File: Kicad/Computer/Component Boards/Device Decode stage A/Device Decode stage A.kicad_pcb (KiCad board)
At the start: 2 copper layers, 26.7 x 59.7 mm, 26 parts, among them IC1 AP7365-33WG-7, IC12 SN74LVC1G10DBVR, IC13 74LVC04APW,118, IC16 74LVC02APW,118, IC2 74LVC138APW-Q100J, IC3 74LVC02APW,118, IC4 74LVC1G32GV,125, IC5 74LVC02APW,118, IC6 74LVC3G34DP,125, IC7 SN74F521NSR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

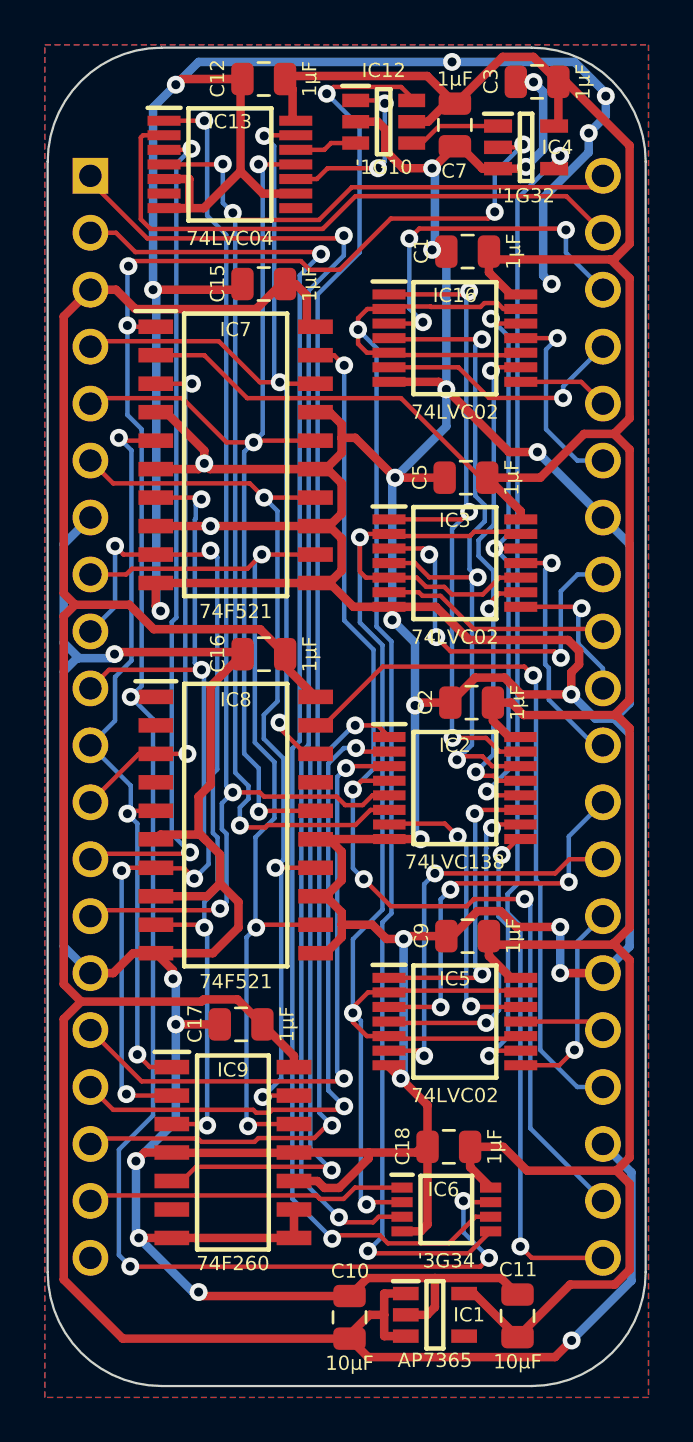
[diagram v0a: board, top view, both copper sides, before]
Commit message: Added Device Decode stage B.
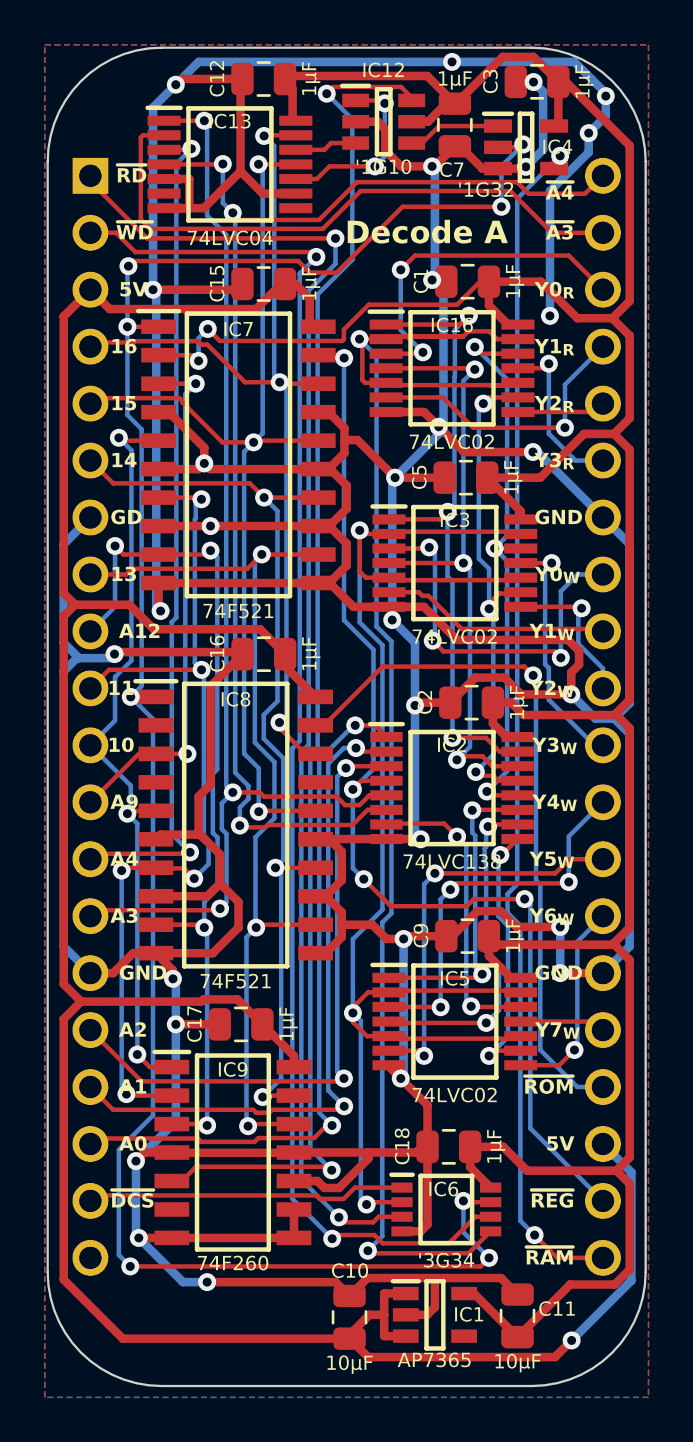
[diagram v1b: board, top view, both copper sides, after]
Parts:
- moved IC16 1.35 mm to (105.0, 67.0)
- moved C1 1.34 mm to (105.7, 63.1)
- moved IC2 0.13 mm to (105.0, 85.7)
- moved IC7 0.13 mm to (95.5, 70.9)
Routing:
- net /~{RD}: track 63.9 -> 67.9 mm
- net /Y1: track 31.3 -> 28.2 mm
- net /GND: track 384.5 -> 382.4 mm
- net /Y0: track 31.0 -> 29.1 mm
- net /Y2: track 24.3 -> 22.6 mm
- net /~{Y3+R}: track 9.03 -> 7.49 mm
- net /~{Y1+R}: track 11.4 -> 12.8 mm
- net /3.3V: track 144.9 -> 145.8 mm, vias 0 -> 2
- net /~{RD}_{IN}: track 60.7 -> 60.0 mm
- net /~{Device RAM}: track 54.4 -> 53.8 mm
- net /~{Y2+R}: track 4.07 -> 3.42 mm
- net /Y3: track 26.5 -> 25.9 mm
- net /~{Y0+R}: track 16.1 -> 15.7 mm, vias 3 -> 2
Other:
- board text added: "10"
- board text added: "11"
- board text added: "13"
- board text added: "14"
- board text added: "15"
- board text added: "16"
- board text added: "5V"
- board text added: "A0"
- board text added: "A1"
- board text added: "A12"
- board text added: "A2"
- board text added: "A3"
- board text added: "A4"
- board text added: "A9"
- board text added: "Decode A"
- board text added: "GD"
- board text added: "GND"
- board text added: "Y0_{R}"
- board text added: "Y0_{W}"
- board text added: "Y1_{R}"
- board text added: "Y1_{W}"
- board text added: "Y2_{R}"
- board text added: "Y2_{W}"
- board text added: "Y3_{R}"
- board text added: "Y3_{W}"
- board text added: "Y4_{W}"
- board text added: "Y5_{W}"
- board text added: "Y6_{W}"
- board text added: "Y7_{W}"
- board text added: "~{A3}"
- board text added: "~{A4}"
- board text added: "~{DCS}"
- board text added: "~{RAM}"
- board text added: "~{RD}"
- board text added: "~{REG}"
- board text added: "~{ROM}"
- board text added: "~{WD}"

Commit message: Bit of device decode fix-up.
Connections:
- net /Y0 renamed /~{Y0}
- net /Y1 renamed /~{Y1}
- net /Y2 renamed /~{Y2}
- net /Y3 renamed /~{Y3}
- net /Y4 renamed /~{Y4}
- net /Y5 renamed /~{Y5}
- net /Y6 renamed /~{Y6}
- net /Y7 renamed /~{Y7}
- net /~{Y0+R} renamed /Y0+R
- net /~{Y0+W} renamed /Y0+W
- net /~{Y1+R} renamed /Y1+R
- net /~{Y1+W} renamed /Y1+W
- net /~{Y2+R} renamed /Y2+R
- net /~{Y2+W} renamed /Y2+W
- net /~{Y3+R} renamed /Y3+R
- net /~{Y3+W} renamed /Y3+W
- net /~{Y4+W} renamed /Y4+W
- net /~{Y5+W} renamed /Y5+W
- net /~{Y6+W} renamed /Y6+W
- net /~{Y7+W} renamed /Y7+W

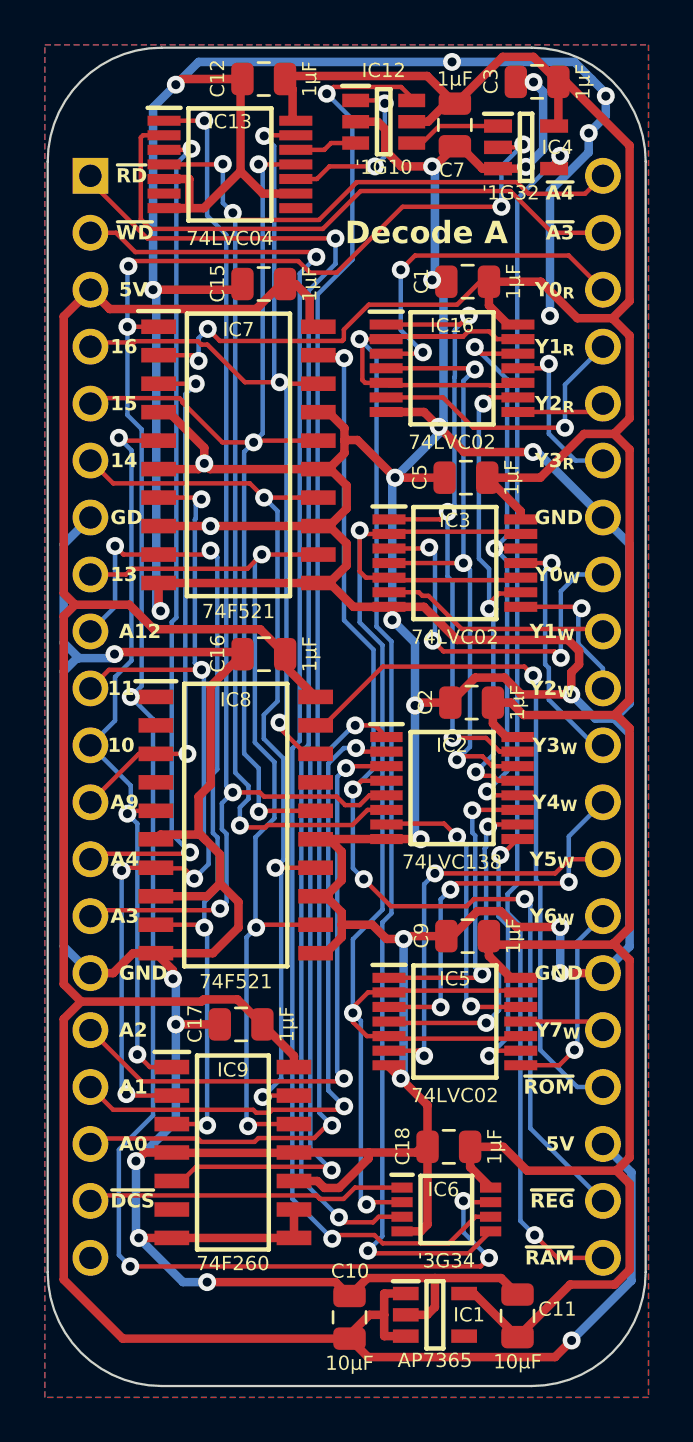
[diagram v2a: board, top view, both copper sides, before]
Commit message: Updated the Signal Buffer to be a Data and Signal Buffer.
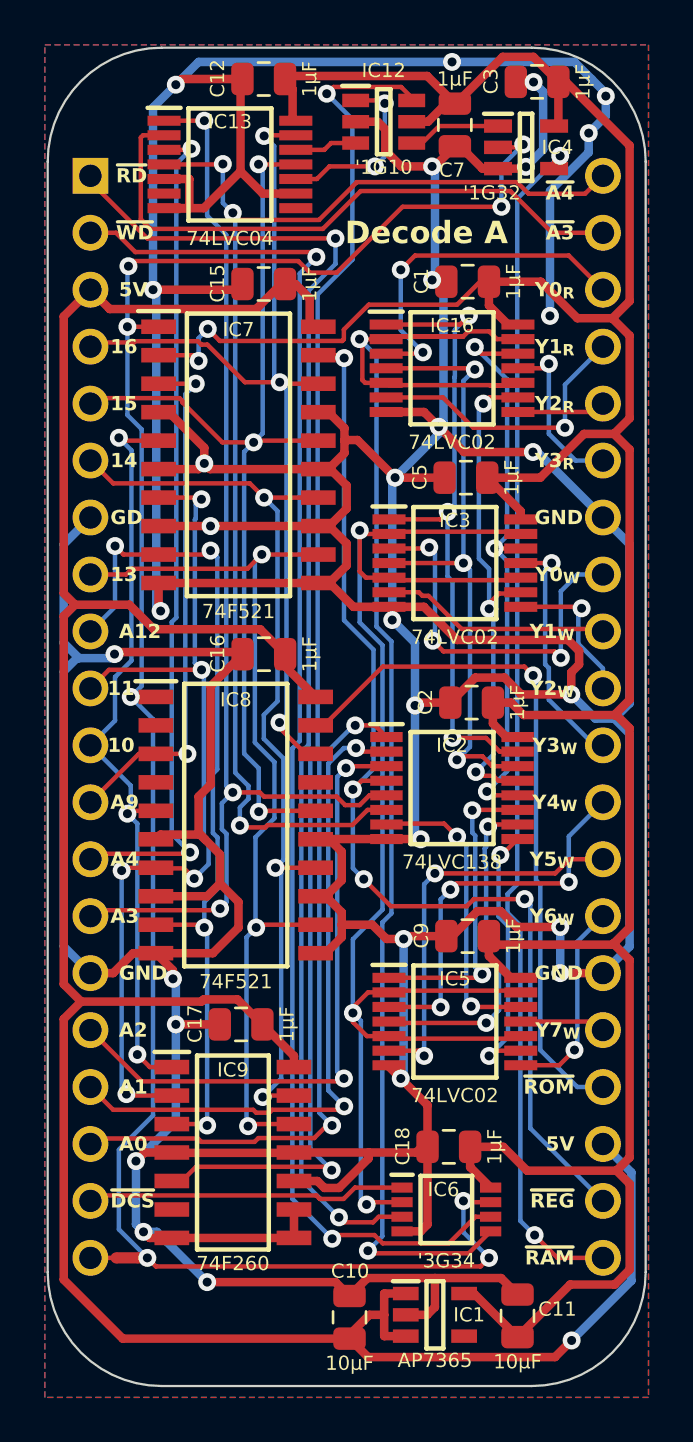
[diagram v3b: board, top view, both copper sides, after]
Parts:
- added NT1: NetTie_2, NetTie:NetTie-2_SMD_Pad0.5mm, F.Cu at (90.6, 106.7)
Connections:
- J1 pad 20: unconnected-(J1-Pin_20-Pad20) -> /~{Device Select} _{OUT}
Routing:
- net /~{Device Select} _{OUT}: track 0.00 -> 1.15 mm

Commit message: Include ROM read and write clock holds.
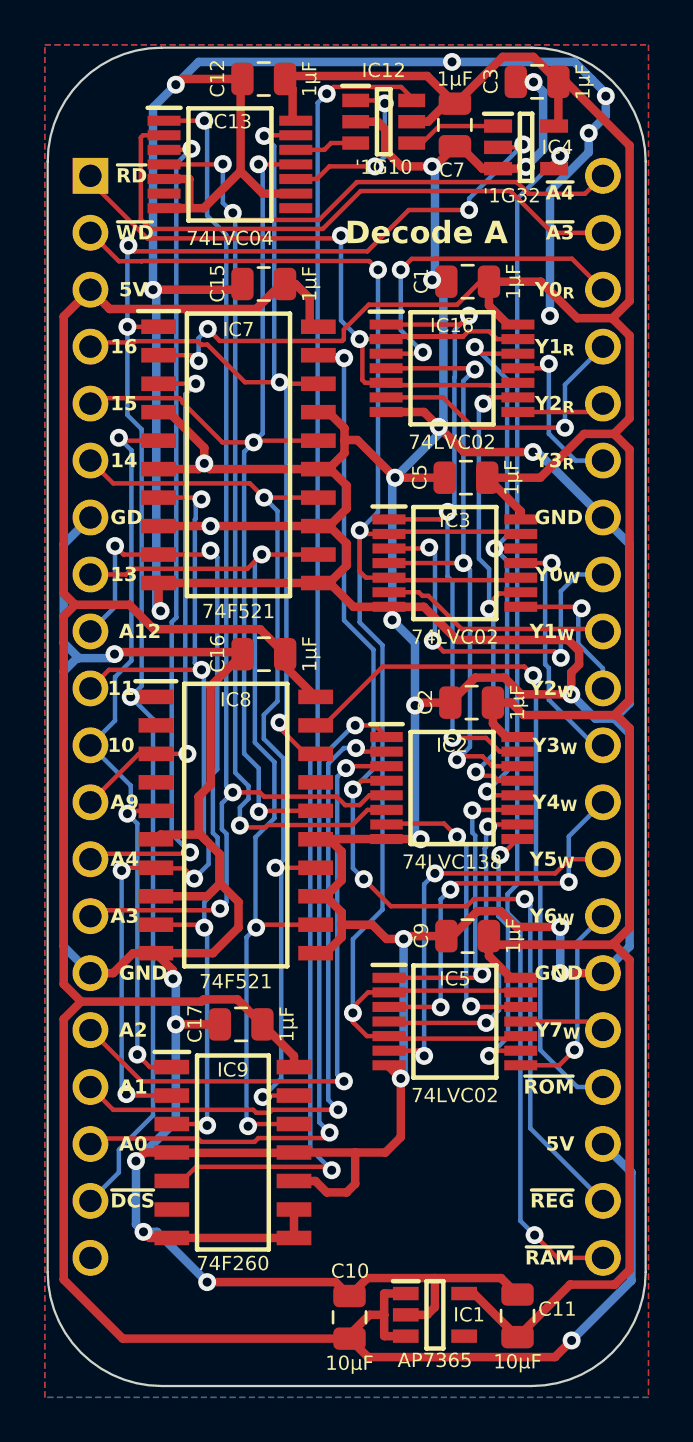
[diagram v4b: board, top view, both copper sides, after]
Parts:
- removed C18: 1μF, SamacSys_Parts:C_0805
- removed IC6: 74LVC3G34DP,125, SamacSys_Parts:SOP65P400X110-8N
- removed NT1: NetTie_2, NetTie:NetTie-2_SMD_Pad0.5mm
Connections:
- J1 pad 1: /~{RD}_{IN} -> /~{RD}
- J1 pad 19: /~{Device Select}_{ IN} -> /~{Device Select}
- J1 pad 2: /~{WD}_{IN} -> /~{WD}
- J1 pad 20: /~{Device Select} _{OUT} -> unconnected-(J1-Pin_20-Pad20)
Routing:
- net /~{WD}_{IN}: track 63.3 -> 0.00 mm, vias 2 -> 0
- net /~{RD}_{IN}: track 60.0 -> 0.00 mm, vias 2 -> 0
- net /~{RD}: track 67.9 -> 37.5 mm
- net /~{Device Select}: track 91.5 -> 68.3 mm, vias 8 -> 5
- net /~{WD}: track 64.5 -> 79.5 mm
- net /~{Device Select}_{ IN}: track 13.9 -> 0.00 mm
- net /3.3V: track 145.8 -> 136.1 mm
- net /GND: track 382.0 -> 375.8 mm
- net /~{Device Select} _{OUT}: track 1.15 -> 0.00 mm
- net /~{A10...+...A14}: track 61.0 -> 60.0 mm

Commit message: Added version number to component boards.
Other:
- board text added: "V0"
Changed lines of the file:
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@@
     (effects (font (size 0.635 0.635) (thickness 0.15) bold) (justify right))
+  )
+  (gr_text "V0" (at 104.14 103.378) (layer "F.SilkS" knockout)
+    (effects (font (size 1 1) (thickness 0.2) bold))
   )
   (gr_text "GND" (at 90.17 93.98) (layer "F.SilkS")

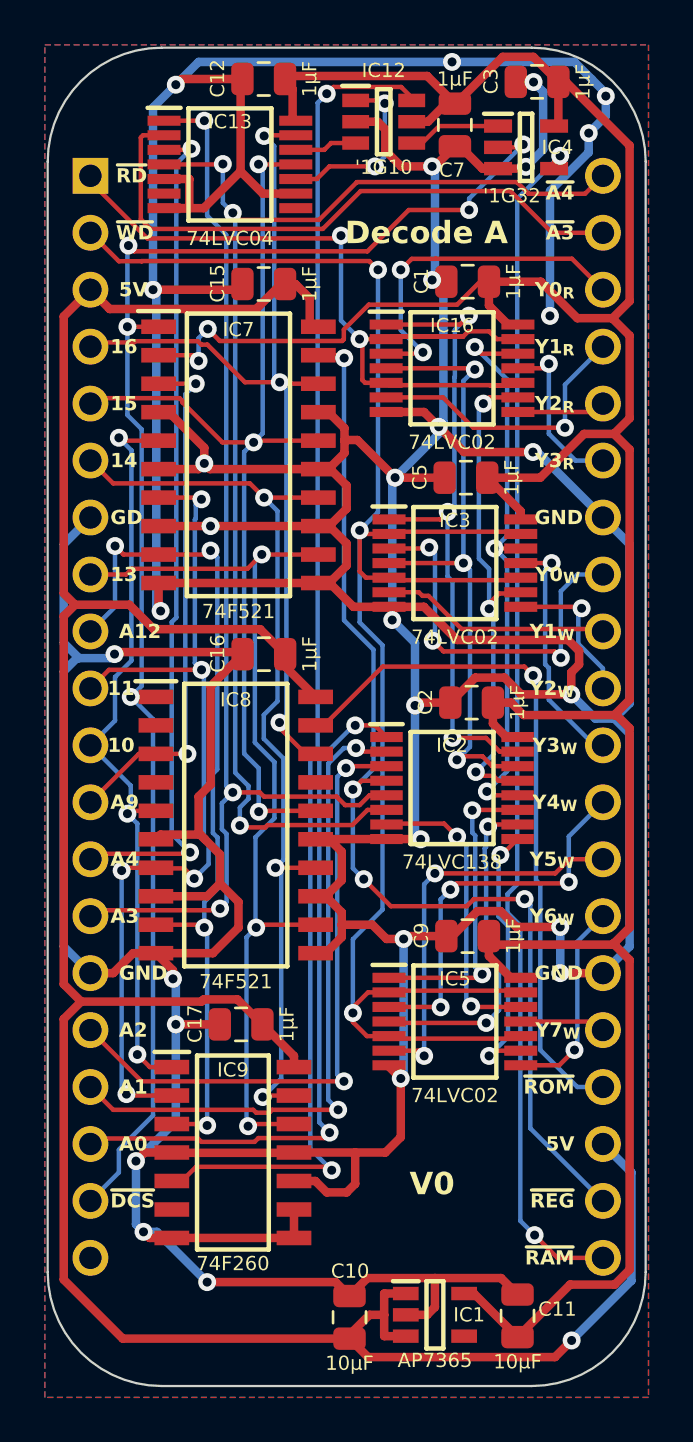
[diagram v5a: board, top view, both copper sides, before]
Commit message: Standardising DIP board layouts.
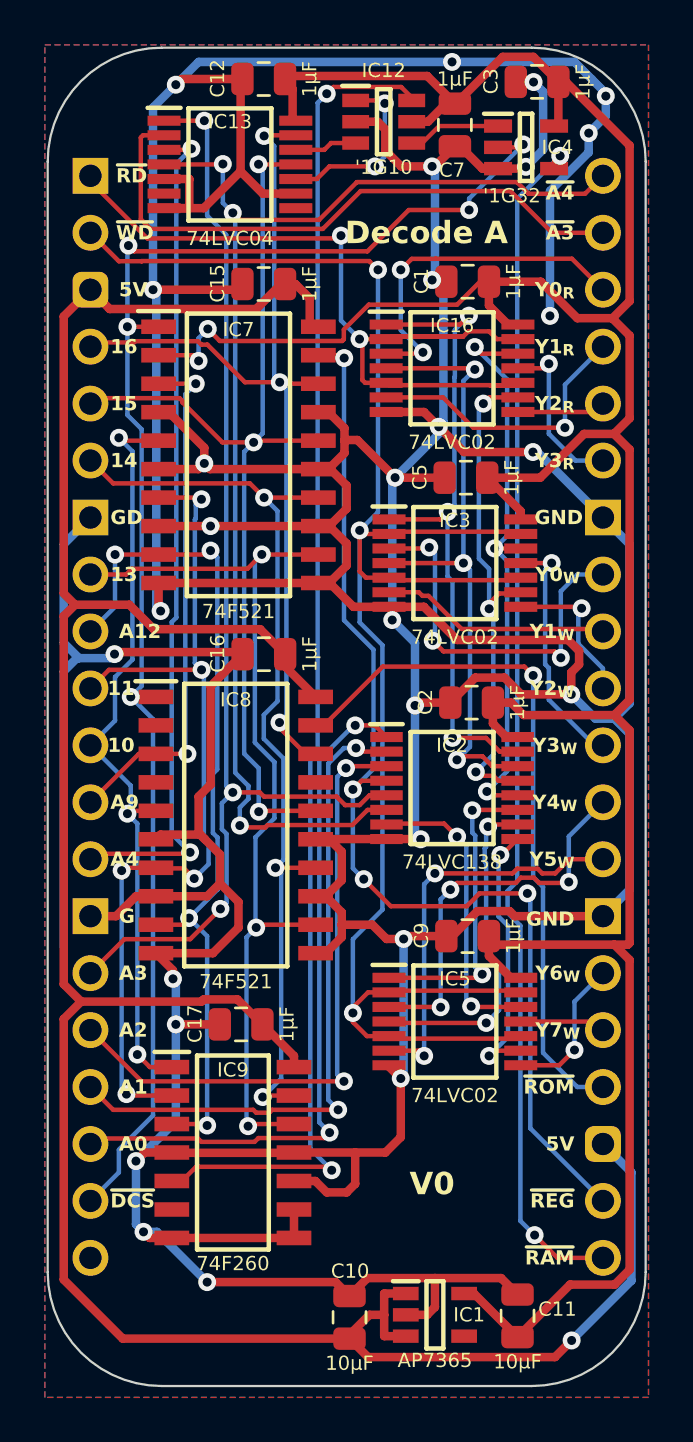
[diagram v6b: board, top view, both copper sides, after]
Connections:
- J1 pad 14: /A3 -> /GND
- J1 pad 15: /GND -> /A3
- J1 pad 26: /GND -> /Y6+W
- J1 pad 27: /Y6+W -> /GND
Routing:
- net /GND: track 375.8 -> 369.3 mm, vias 30 -> 28
- net /Y6+W: track 9.17 -> 6.63 mm
- net /A3: track 50.7 -> 52.1 mm
- net /A12: track 38.8 -> 38.2 mm
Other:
- board text added: "G"

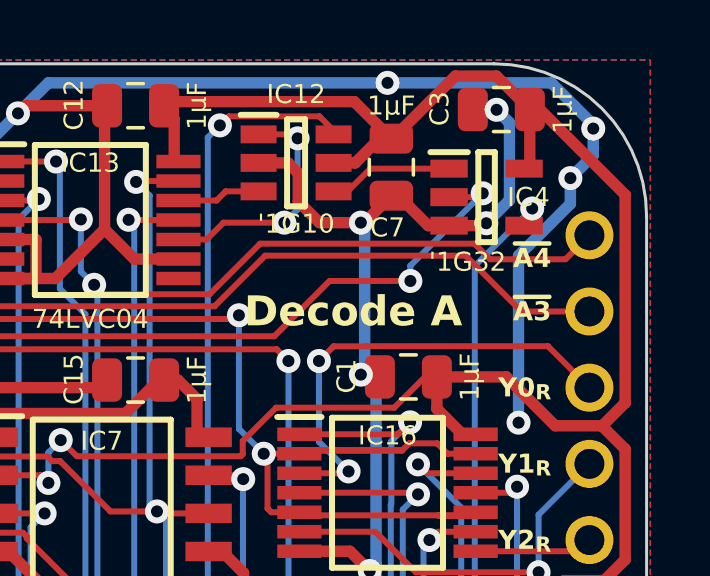
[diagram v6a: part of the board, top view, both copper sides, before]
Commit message: Added pull-ups to the MPU MPU Breakout.
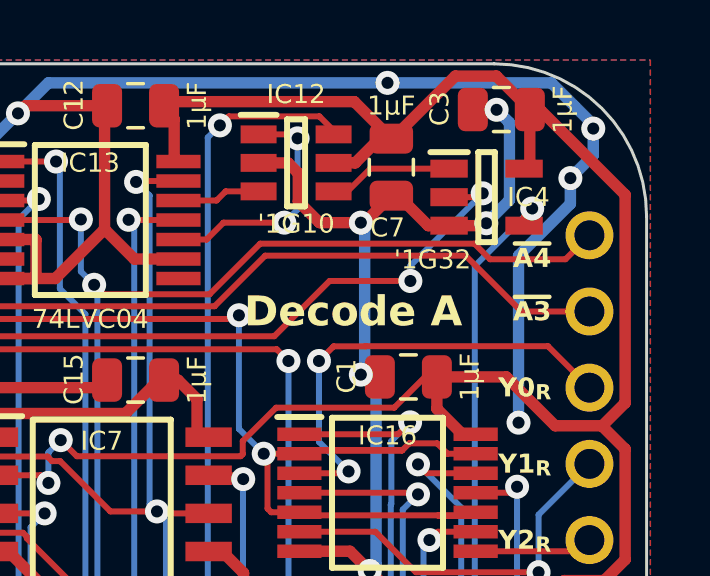
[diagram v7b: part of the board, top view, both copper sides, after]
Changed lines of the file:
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@@
         (effects (font (size 0.635 0.635) (thickness 0.15)))
     )
-    (fp_text user "${Silkscreen}" (at -0.635 2.159) (layer "F.SilkS")
+    (fp_text user "${Silkscreen}" (at -1.8034 2.0828) (layer "F.SilkS")
         (effects (font (size 0.635 0.635) (thickness 0.15)))
     )
